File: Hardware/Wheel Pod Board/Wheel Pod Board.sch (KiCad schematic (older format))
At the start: 30 parts, among them J1 Conn_RJ-45, P1 UIM240XX_Stepper_Conn, P2 RS232, P3 ST_SWD_Connector, P5 BATT, P6 SyRen Pwr, U1 STM32F401RCT6, U2 SN75176BDR, U3 ZXCT1107, U4 ZXCT1107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

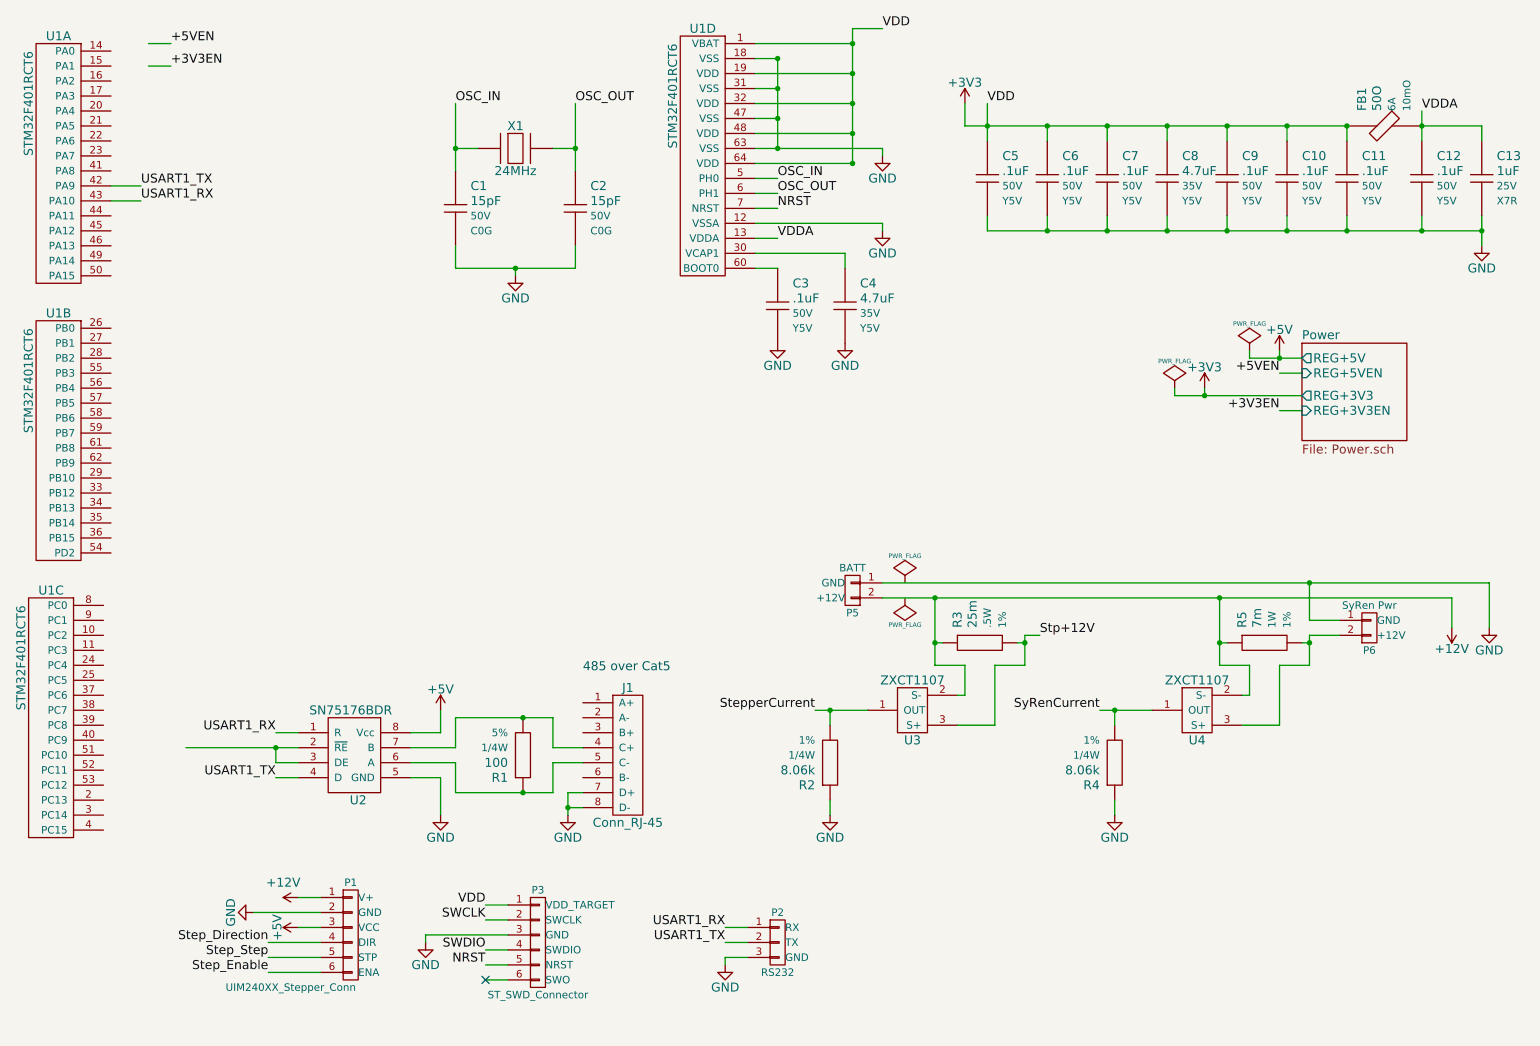
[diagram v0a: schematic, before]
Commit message: Reroute 3V3 and 5V through cat5, remove regs
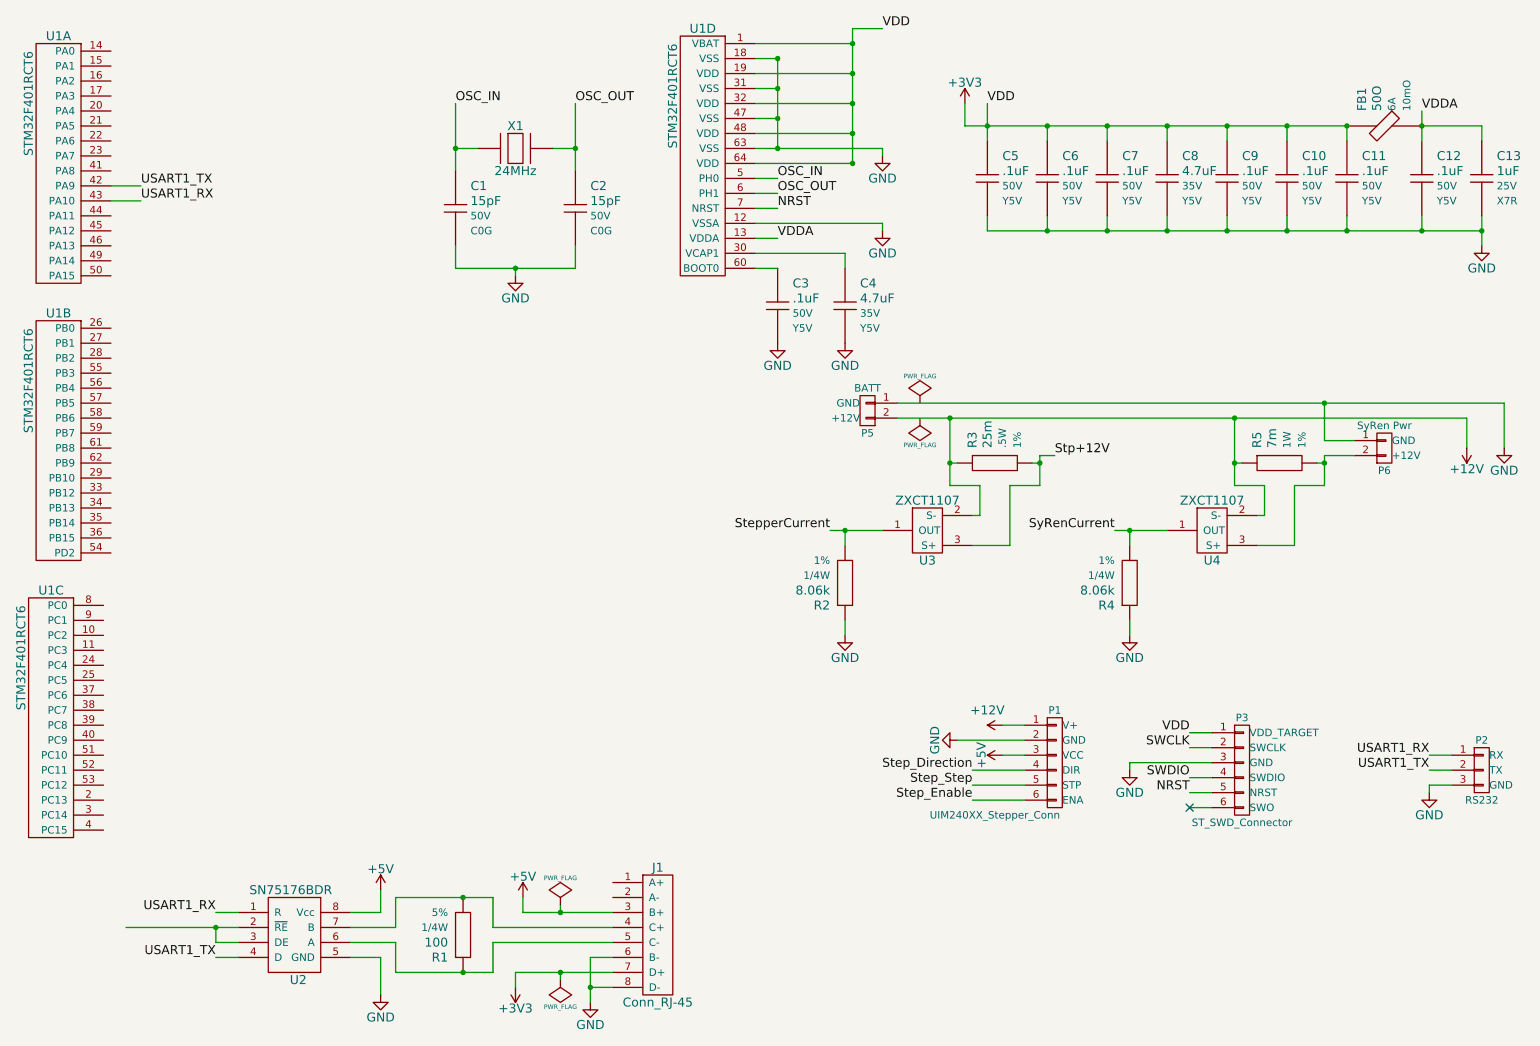
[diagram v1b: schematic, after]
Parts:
- J1: footprint Connect:RJ45_8 -> MAVRIC_footprints:Molex_RJ45_0437438101
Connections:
- net +3V3: now also J1.7 (D+)
- net +5V: now also J1.3 (B+)
- net GND: now also J1.6 (B-); no longer J1.7 (D+)
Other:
- note removed: "485 over Cat5"
- moved on the sheet: J1, P1, P2, P3, P5, P6, R1, R2, R3, R4, R5, U2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

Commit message: Make STM32 connections, fix DRC errors
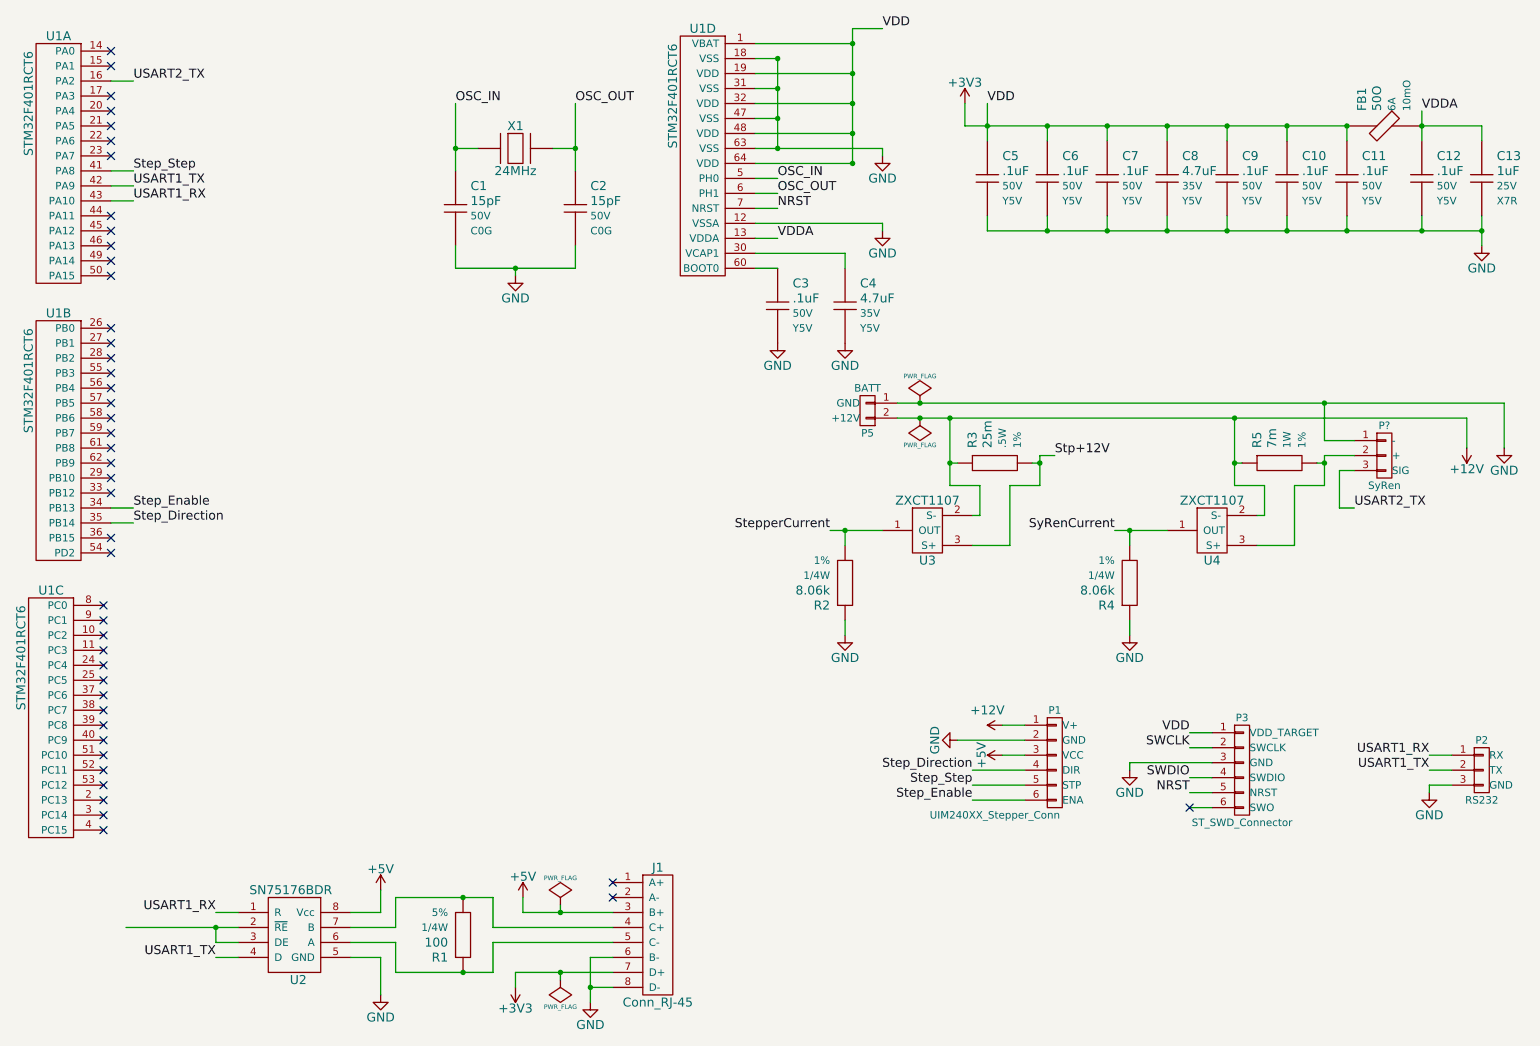
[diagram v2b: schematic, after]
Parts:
- removed P6: SyRen Pwr, MAVRIC_footprints:1x2_SMD_header, symbol BATT
- added P?: SyRen, symbol SERVO
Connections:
- net GND: now also P?.1 (-)
- net Step_Direction: now also U1.35 (PB14)
- net Step_Enable: now also U1.34 (PB13)
- net Step_Step: now also U1.41 (PA8)
- net USART2_TX: now reaches U1.16 (PA2)
- net USART2_TX: now also P?.3 (SIG)
- net at R5.2, U4.3 (S+): now also P?.2 (+)
- no-connect marks 1 -> 45
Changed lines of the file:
@@
-$Comp
-L STM32F401RCT6 U1
-U 1 1 54E6BCED
-P 1450 1150
-F 0 "U1" H 1300 1250 60  0000 C CNN
-F 1 "STM32F401RCT6" V 1100 800 60  0000 C CNN
-F 2 "Housings_QFP:LQFP-64_10x10mm_Pitch0.5mm" H 1450 -450 60  0001 C CNN
-F 3 "" H 1450 -450 60  0000 C CNN
-	1    1450 1150
-	1    0    0    -1
-$EndComp
 $Comp
 L STM32F401RCT6 U1
@@
 	6800 1800 6800 1850
 Connection ~ 6600 1300
-Wire Wire Line
-	5950 1100 6600 1100
 Connection ~ 6600 1100
 Wire Wire Line
@@
 	9000 6100 8850 6100
 Wire Wire Line
-	9000 6000 8850 6000
-Wire Wire Line
-	9000 5800 8850 5800
-Wire Wire Line
 	9000 5900 8450 5900
 Wire Wire Line
@@
 $EndComp
 $Comp
-L GND #PWR015
+L GND #PWR014
 U 1 1 54F91E0A
 P 10800 2450
-F 0 "#PWR015" H 10800 2200 60  0001 C CNN
+F 0 "#PWR014" H 10800 2200 60  0001 C CNN
 F 1 "GND" H 10800 2300 60  0000 C CNN
 F 2 "" H 10800 2450 60  0000 C CNN
@@
 $EndComp
 $Comp
-L GND #PWR016
+L GND #PWR015
 U 1 1 54F97284
 P 8450 5050
-F 0 "#PWR016" H 8450 4800 60  0001 C CNN
+F 0 "#PWR015" H 8450 4800 60  0001 C CNN
 F 1 "GND" H 8450 4900 60  0000 C CNN
 F 2 "" H 8450 5050 60  0000 C CNN
@@
 	10950 3500 10950 3800
 $Comp
-L GND #PWR017
+L GND #PWR016
 U 1 1 54F987F3
 P 10950 3800
-F 0 "#PWR017" H 10950 3550 60  0001 C CNN
+F 0 "#PWR016" H 10950 3550 60  0001 C CNN
 F 1 "GND" H 10950 3650 60  0000 C CNN
 F 2 "" H 10950 3800 60  0000 C CNN
@@
 	1    0    0    -1
 $EndComp
-$Comp
-L BATT P6
-U 1 1 54F99637
-P 10150 3800
-F 0 "P6" H 10150 3950 50  0000 C CNN
-F 1 "SyRen Pwr" H 10150 3650 50  0000 C CNN
-F 2 "MAVRIC_footprints:1x2_SMD_header" H 10150 3800 60  0001 C CNN
-F 3 "" H 10150 3800 60  0000 C CNN
-	1    10150 3800
-	1    0    0    1
-$EndComp
 Wire Wire Line
 	7850 3850 7950 3850
@@
 Connection ~ 9150 3600
 $Comp
-L +12V #PWR018
+L +12V #PWR017
 U 1 1 54F9E120
 P 10700 3800
-F 0 "#PWR018" H 10700 3650 60  0001 C CNN
+F 0 "#PWR017" H 10700 3650 60  0001 C CNN
 F 1 "+12V" H 10700 3940 60  0000 C CNN
 F 2 "" H 10700 3800 60  0000 C CNN
@@
 $EndComp
 $Comp
-L PWR_FLAG #FLG019
+L PWR_FLAG #FLG018
 U 1 1 54F9E134
 P 7050 3600
-F 0 "#FLG019" H 7050 3695 30  0001 C CNN
+F 0 "#FLG018" H 7050 3695 30  0001 C CNN
 F 1 "PWR_FLAG" H 7050 3780 30  0000 C CNN
 F 2 "" H 7050 3600 60  0000 C CNN
@@
 $EndComp
 $Comp
-L PWR_FLAG #FLG020
+L PWR_FLAG #FLG019
 U 1 1 54F9E417
 P 7050 3500
-F 0 "#FLG020" H 7050 3595 30  0001 C CNN
+F 0 "#FLG019" H 7050 3595 30  0001 C CNN
 F 1 "PWR_FLAG" H 7050 3680 30  0000 C CNN
 F 2 "" H 7050 3500 60  0000 C CNN
@@
 Connection ~ 9750 3500
 $Comp
-L +3V3 #PWR021
+L +3V3 #PWR020
 U 1 1 54FA32A7
 P 7350 1500
-F 0 "#PWR021" H 7350 1350 60  0001 C CNN
+F 0 "#PWR020" H 7350 1350 60  0001 C CNN
 F 1 "+3V3" H 7350 1640 60  0000 C CNN
 F 2 "" H 7350 1500 60  0000 C CNN
@@
 $EndComp
 $Comp
-L +5V #PWR022
+L +5V #PWR021
 U 1 1 54FA4C38
 P 3450 6750
-F 0 "#PWR022" H 3450 6600 60  0001 C CNN
+F 0 "#PWR021" H 3450 6600 60  0001 C CNN
 F 1 "+5V" H 3450 6890 60  0000 C CNN
 F 2 "" H 3450 6750 60  0000 C CNN
@@
 	1    0    0    -1
 $EndComp
-Text Label 1850 2150 0    60   ~ 0
+Text Label 1800 2150 0    60   ~ 0
 USART1_RX
-Text Label 1850 2050 0    60   ~ 0
+Text Label 1800 2050 0    60   ~ 0
 USART1_TX
 Wire Wire Line
-	1850 2150 1650 2150
-Wire Wire Line
-	1850 2050 1650 2050
+	1800 2150 1650 2150
+Wire Wire Line
+	1800 2050 1650 2050
 Text Label 7950 3850 0    60   ~ 0
 Stp+12V
 $Comp
-L +5V #PWR023
+L +5V #PWR022
 U 1 1 54FACDEA
 P 7600 5850
-F 0 "#PWR023" H 7600 5700 60  0001 C CNN
+F 0 "#PWR022" H 7600 5700 60  0001 C CNN
 F 1 "+5V" H 7600 5990 60  0000 C CNN
 F 2 "" H 7600 5850 60  0000 C CNN
@@
 	10450 6050 10450 6100
 $Comp
-L GND #PWR024
+L GND #PWR023
 U 1 1 54FB0646
 P 10450 6100
-F 0 "#PWR024" H 10450 5850 60  0001 C CNN
+F 0 "#PWR023" H 10450 5850 60  0001 C CNN
 F 1 "GND" H 10450 5950 60  0000 C CNN
 F 2 "" H 10450 6100 60  0000 C CNN
@@
 	4400 6900 5000 6900
 $Comp
-L PWR_FLAG #FLG?
+L PWR_FLAG #FLG024
 U 1 1 54F9E182
 P 4650 6850
-F 0 "#FLG?" H 4650 6945 30  0001 C CNN
+F 0 "#FLG024" H 4650 6945 30  0001 C CNN
 F 1 "PWR_FLAG" H 4650 7030 30  0000 C CNN
 F 2 "" H 4650 6850 60  0000 C CNN
@@
 Connection ~ 4850 7400
 $Comp
-L GND #PWR?
+L GND #PWR025
 U 1 1 54F9E9CC
 P 4850 7500
-F 0 "#PWR?" H 4850 7250 60  0001 C CNN
+F 0 "#PWR025" H 4850 7250 60  0001 C CNN
 F 1 "GND" H 4850 7350 60  0000 C CNN
 F 2 "" H 4850 7500 60  0000 C CNN
@@
 Wire Wire Line
 	4200 7100 5000 7100
+Wire Wire Line
+	1650 1350 1800 1350
+Text Label 1800 1350 0    60   ~ 0
+USART2_TX
+$Comp
+L STM32F401RCT6 U1
+U 1 1 54E6BCED
+P 1450 1150
+F 0 "U1" H 1300 1250 60  0000 C CNN
+F 1 "STM32F401RCT6" V 1100 800 60  0000 C CNN
+F 2 "Housings_QFP:LQFP-64_10x10mm_Pitch0.5mm" H 1450 -450 60  0001 C CNN
+F 3 "" H 1450 -450 60  0000 C CNN
+	1    1450 1150
+	1    0    0    -1
+$EndComp
+NoConn ~ 1650 1150
+NoConn ~ 1650 1250
+NoConn ~ 1650 1450
+NoConn ~ 1650 1550
+NoConn ~ 1650 1650
+NoConn ~ 1650 1750
+NoConn ~ 1650 1850
+NoConn ~ 1650 2250
+NoConn ~ 1650 2350
+NoConn ~ 1650 2450
+NoConn ~ 1650 2550
+NoConn ~ 1650 2650
+NoConn ~ 1650 3000
+NoConn ~ 1650 3100
+NoConn ~ 1650 3200
+NoConn ~ 1650 3300
+NoConn ~ 1650 3400
+NoConn ~ 1650 3500
+NoConn ~ 1650 3600
+NoConn ~ 1650 3700
+NoConn ~ 1650 3800
+NoConn ~ 1650 3900
+NoConn ~ 1650 4000
+NoConn ~ 1650 4100
+NoConn ~ 1650 4400
+NoConn ~ 1650 4500
+NoConn ~ 1600 4850
+NoConn ~ 1600 4950
+NoConn ~ 1600 5050
+NoConn ~ 1600 5150
+NoConn ~ 1600 5250
+NoConn ~ 1600 5350
+NoConn ~ 1600 5450
+NoConn ~ 1600 5550
+NoConn ~ 1600 5650
+NoConn ~ 1600 5750
+NoConn ~ 1600 5850
+NoConn ~ 1600 5950
+NoConn ~ 1600 6050
+NoConn ~ 1600 6150
+NoConn ~ 1600 6250
+NoConn ~ 1600 6350
+NoConn ~ 5000 6700
+NoConn ~ 5000 6800
+Wire Wire Line
+	5950 1100 6600 1100
+Connection ~ 7050 3500
+Connection ~ 7050 3600
+Wire Wire Line
+	9000 6000 8850 6000
+Wire Wire Line
+	8850 5800 9000 5800
+Text Label 1800 4300 0    60   ~ 0
+Step_Direction
+Text Label 1800 1950 0    60   ~ 0
+Step_Step
+Text Label 1800 4200 0    60   ~ 0
+Step_Enable
+Wire Wire Line
+	1650 4300 1800 4300
+Wire Wire Line
+	1650 1950 1800 1950
+Wire Wire Line
+	1650 4200 1800 4200
+$Comp
+L SERVO P?
+U 1 1 54FB2C02
+P 10150 3850
+F 0 "P?" H 10150 4050 50  0000 C CNN
+F 1 "SyRen" H 10150 3650 50  0000 C CNN
+F 2 "" H 10150 3850 60  0000 C CNN
+F 3 "" H 10150 3850 60  0000 C CNN
+	1    10150 3850
+	1    0    0    -1
+$EndComp
+Wire Wire Line
+	9950 3950 9850 3950
+Wire Wire Line
+	9850 3950 9850 4200
+Wire Wire Line
+	9850 4200 9950 4200
+Text Label 9950 4200 0    60   ~ 0
+USART2_TX
 $EndSCHEMATC

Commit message: Update cube, make connections to microcontroller
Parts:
- P4: renamed from P?; footprint (none) -> MAVRIC_footprints:1x3_SMD_header
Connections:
- net SWCLK: now also U1.49 (PA14)
- net SWDIO: now also U1.46 (PA13)
- net StepperCurrent: now also U1.14 (PA0)
- net SyRenCurrent: now also U1.15 (PA1)
- no-connect marks 45 -> 41
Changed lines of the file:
@@
 	1    0    0    -1
 $EndComp
-NoConn ~ 1650 1150
-NoConn ~ 1650 1250
 NoConn ~ 1650 1450
 NoConn ~ 1650 1550
@@
 NoConn ~ 1650 2250
 NoConn ~ 1650 2350
-NoConn ~ 1650 2450
-NoConn ~ 1650 2550
 NoConn ~ 1650 2650
 NoConn ~ 1650 3000
@@
 	1650 4200 1800 4200
 $Comp
-L SERVO P?
+L SERVO P4
 U 1 1 54FB2C02
 P 10150 3850
-F 0 "P?" H 10150 4050 50  0000 C CNN
+F 0 "P4" H 10150 4050 50  0000 C CNN
 F 1 "SyRen" H 10150 3650 50  0000 C CNN
-F 2 "" H 10150 3850 60  0000 C CNN
+F 2 "MAVRIC_footprints:1x3_SMD_header" H 10150 3850 60  0001 C CNN
 F 3 "" H 10150 3850 60  0000 C CNN
 	1    10150 3850
@@
 Text Label 9950 4200 0    60   ~ 0
 USART2_TX
+Text Label 1800 2550 0    60   ~ 0
+SWCLK
+Wire Wire Line
+	1800 2550 1650 2550
+Text Label 1800 2450 0    60   ~ 0
+SWDIO
+Wire Wire Line
+	1800 2450 1650 2450
+Text Label 1800 1150 0    60   ~ 0
+StepperCurrent
+Text Label 1800 1250 0    60   ~ 0
+SyRenCurrent
+Wire Wire Line
+	1650 1250 1800 1250
+Wire Wire Line
+	1800 1150 1650 1150
 $EndSCHEMATC

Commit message: Position components on PCB
Closes #4
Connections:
- net +12V: no longer P1.1 (V+)
- net Stp+12V: now also P1.1 (V+)
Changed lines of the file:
@@
-$EndComp
-$Comp
-L +12V #PWR08
-U 1 1 54F82F59
-P 7600 5650
-F 0 "#PWR08" H 7600 5500 60  0001 C CNN
-F 1 "+12V" V 7700 5750 60  0000 C CNN
-F 2 "" H 7600 5650 60  0000 C CNN
-F 3 "" H 7600 5650 60  0000 C CNN
-	1    7600 5650
-	0    -1   -1   0
 $EndComp
 $Comp
@@
 Wire Wire Line
 	1800 1150 1650 1150
+Text Label 7600 5650 2    60   ~ 0
+Stp+12V
 $EndSCHEMATC
